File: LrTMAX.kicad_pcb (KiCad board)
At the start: 4 copper layers, 100 x 100 mm, 126 parts, among them J1 USB_C_Receptacle_USB2.0, J2 Conn_02x05_Odd_Even, Q1 2N7002, SW1 Tact_SW_8mm, SW10 EC11_SMD, SW11 EC11_SMD, SW12 EC11_SMD, SW13 EC11_SMD, SW14 EC11_SMD, SW15 EC11_SMD, SW16 EC11_SMD, SW17 EC11_SMD, SW2 Tact_SW_8mm, SW20 SW_SPST, SW3 Tact_SW_8mm, SW4 Tact_SW_8mm, SW5 Tact_SW_8mm, SW6 Tact_SW_8mm, SW7 Tact_SW_8mm, SW8 Tact_SW_8mm, U1 STM32F072C8Tx, U3 SSD1306_OLED_0.91, U4 SPX3819M5-L3-3TR

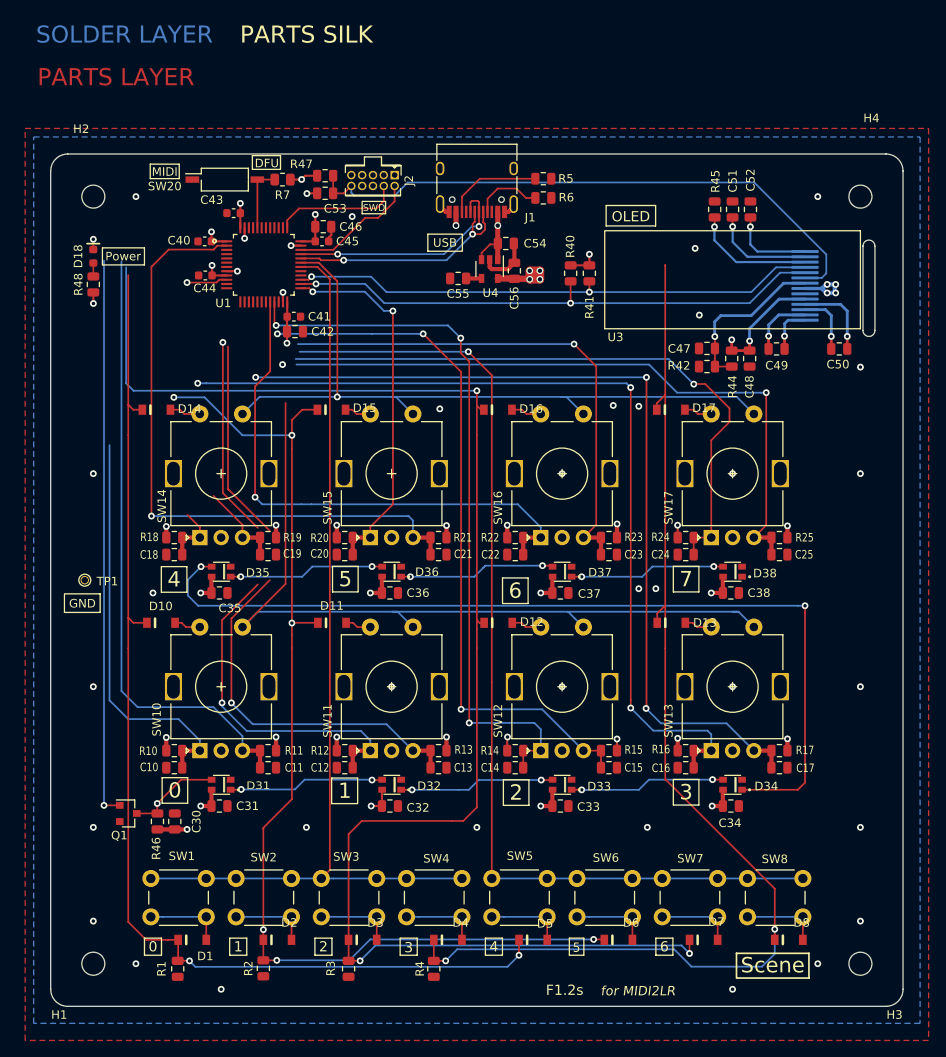
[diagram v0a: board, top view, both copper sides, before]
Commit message: Auto routing completed and some adjustments.
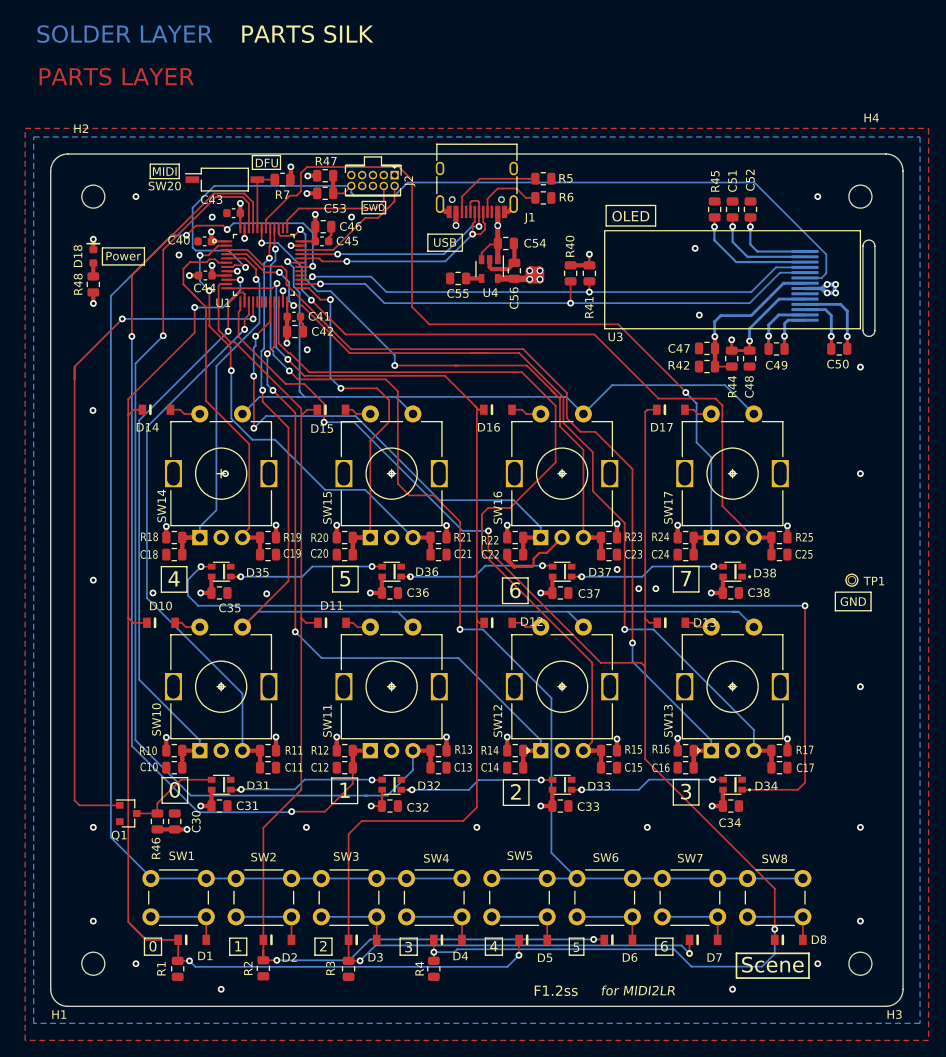
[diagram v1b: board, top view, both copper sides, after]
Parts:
- moved TP1 90.0 mm to (194.0, 150.0)
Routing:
- net /M3: track 136.4 -> 190.0 mm, vias 2 -> 4
- net /ENC1B: track 67.6 -> 119.9 mm
- net /ENC1A: track 63.8 -> 115.3 mm
- net /ENC4A: track 7.32 -> 45.1 mm, vias 0 -> 1
- net /ENC4B: track 10.4 -> 47.1 mm
- net /NRST: track 70.3 -> 104.2 mm, vias 0 -> 1
- net /L0: track 111.2 -> 140.3 mm, vias 0 -> 3
- net /ENC7A: track 73.4 -> 97.6 mm
- net /L2: track 96.2 -> 118.6 mm, vias 0 -> 2
- net /ENC0A: track 47.7 -> 69.3 mm, vias 0 -> 1
- net /ENC5B: track 76.1 -> 57.7 mm, vias 1 -> 3
- net /L1: track 119.3 -> 137.3 mm, vias 1 -> 3
- net /LED_DON: track 65.7 -> 83.0 mm, vias 1 -> 2
- net /M2: track 179.9 -> 163.2 mm, vias 3 -> 4
- net +3V3: track 75.7 -> 91.1 mm, vias 30 -> 31
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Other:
- board text added: "F1.2ss"
- board text removed: "F1.2s"

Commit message: pattern completed
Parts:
- added REF**: LrTMAX-LOGO, LrE-6:LrTMAX-LOGO, F.Cu at (154.3, 194.2)
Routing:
- net GND: track 39.6 -> 47.5 mm, vias 48 -> 55
- net /LED_DON: track 83.0 -> 76.8 mm
- net /ENC3B: track 108.7 -> 106.9 mm
- net /ENC6B: track 70.1 -> 68.7 mm
- net /ENC5B: track 57.7 -> 59.0 mm
- net /M0: track 143.1 -> 142.3 mm, vias 4 -> 6
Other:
- board text added: "F1.2"
- board text added: "SSM"
- board text added: "remov-b4-flight"
- board text removed: "F1.2ss"

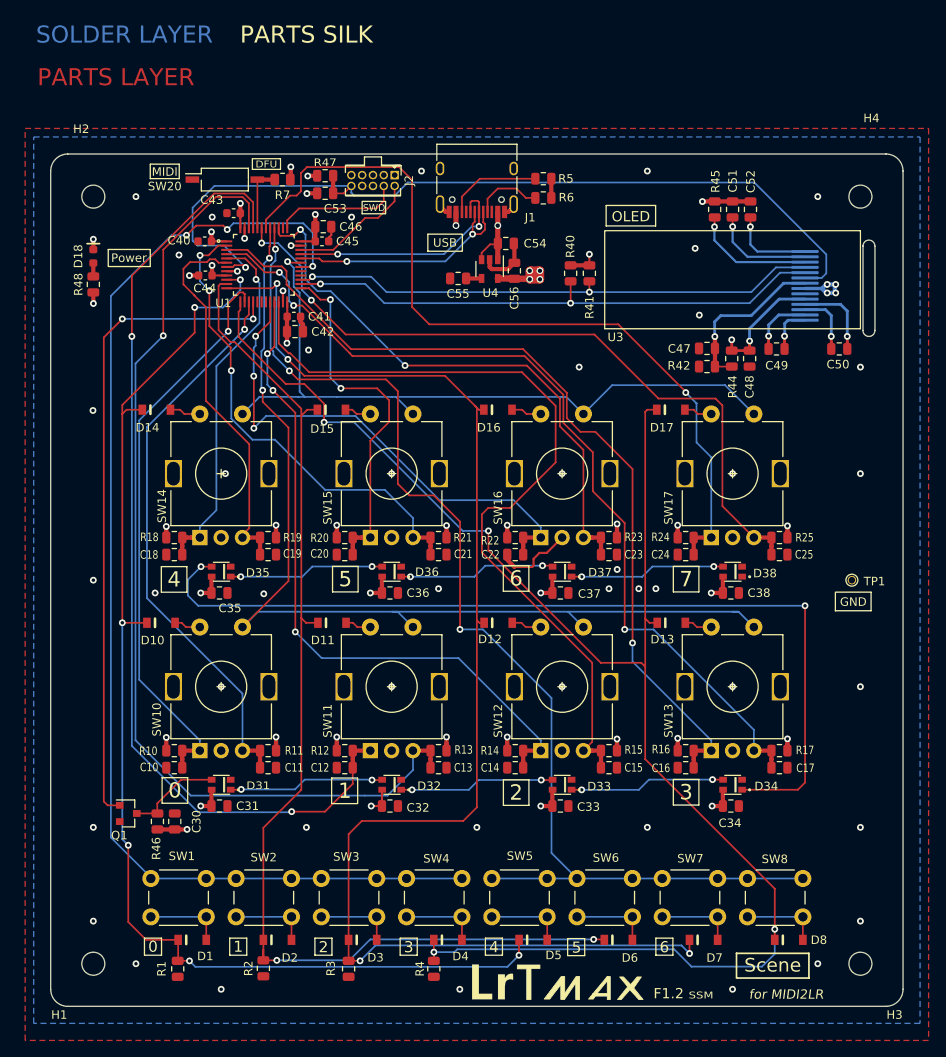
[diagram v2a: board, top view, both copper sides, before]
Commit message: some pattern/sylk refinement
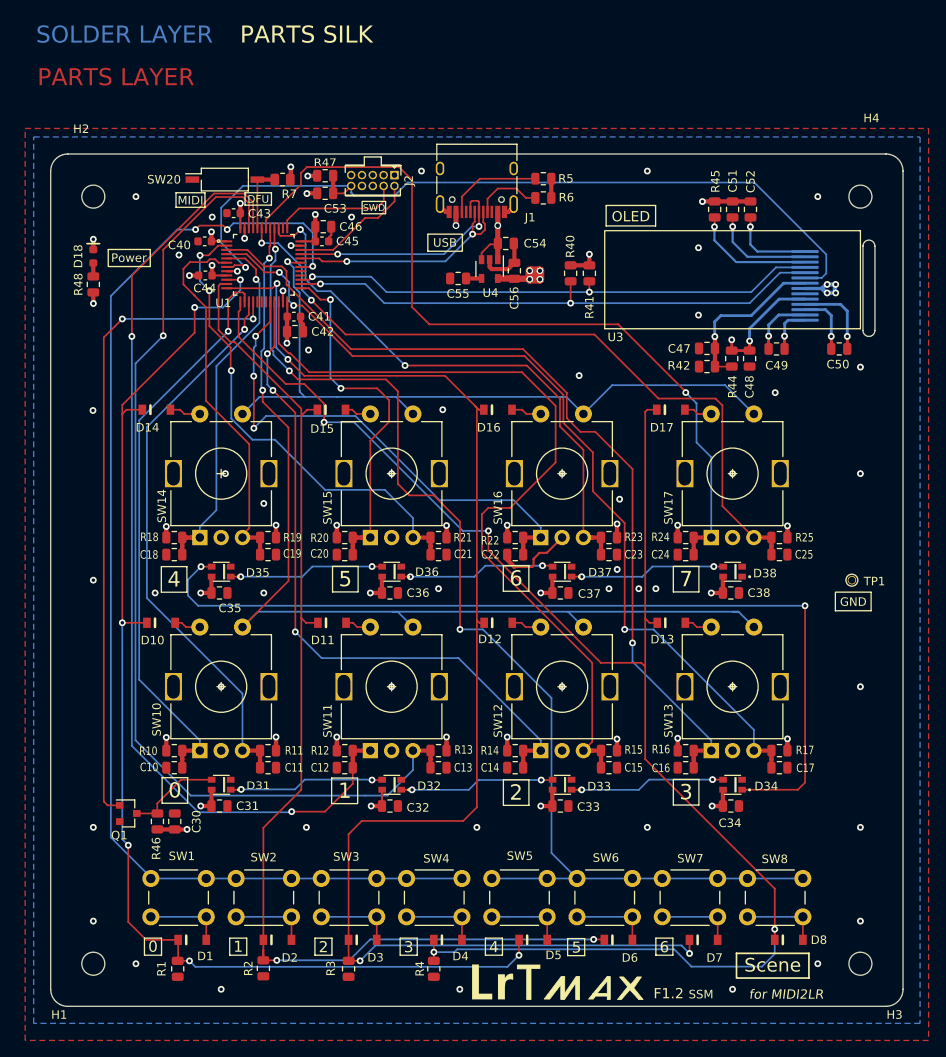
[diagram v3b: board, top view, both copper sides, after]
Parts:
- added G***: LOGO, LrE-6:octocat4r5, B.Cu at (160.5, 195.5)
- moved J2 2.64 mm to (137.8, 103.1)
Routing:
- net /NRST: track 103.8 -> 97.2 mm
- net GND: vias 55 -> 59

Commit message: 1.2SSM board ordered
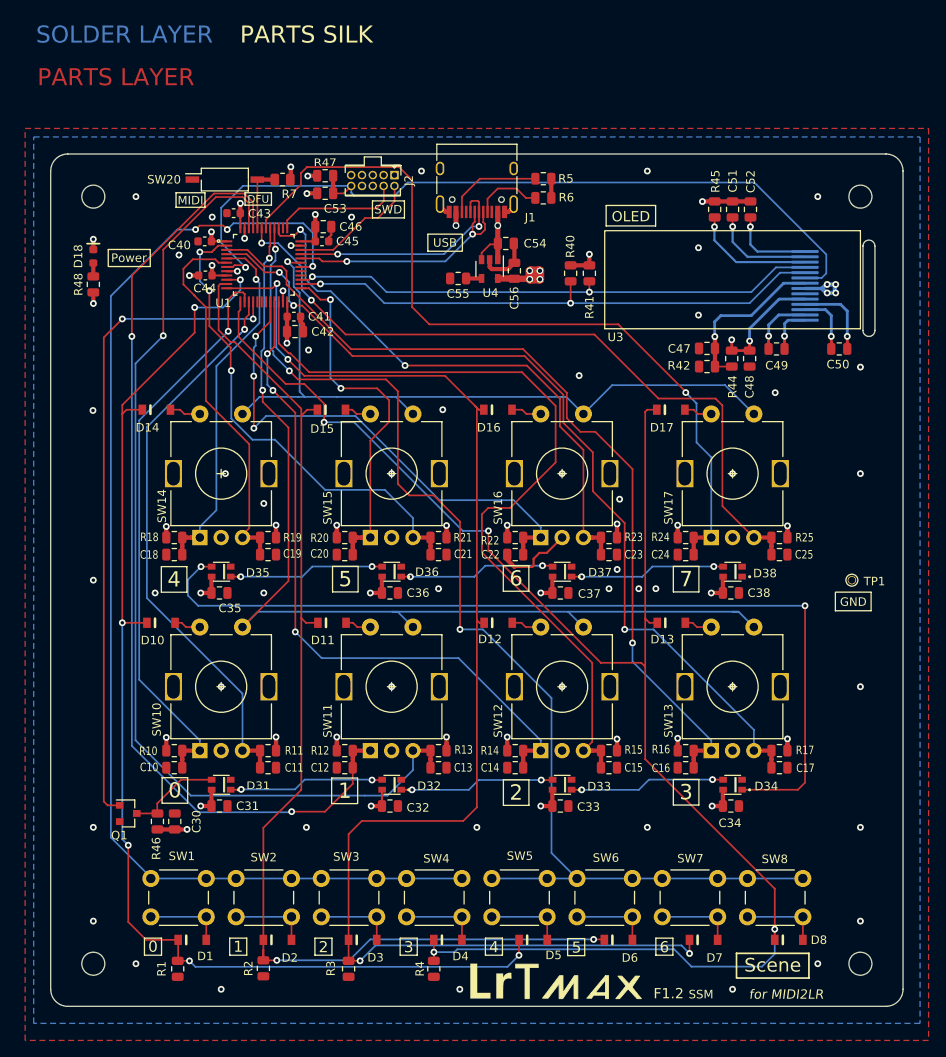
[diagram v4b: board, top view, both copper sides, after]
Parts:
- moved REF** 0.22 mm to (154.1, 194.1)
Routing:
- net /ENC5B: track 59.0 -> 59.6 mm
